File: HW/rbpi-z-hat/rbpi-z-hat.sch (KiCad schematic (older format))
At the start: 0 parts

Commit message: Changes in Sch
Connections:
- net labels added: BQ24313_OUT
- wire segments 66 -> 69
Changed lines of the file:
@@
 $Descr A4 8268 11693 portrait
 encoding utf-8
-Sheet 1 18
+Sheet 1 17
 Title "RasPi Zero NAV Hat"
 Date "2020-08-11"
@@
 $EndSheet
 $Sheet
-S 5200 7900 900  400
-U 5EDADA57
-F0 "MIC5504" 50
-F1 "MIC5504.sch" 50
-F2 "MIC_EN" I L 5200 8100 50
-F3 "MIC_VIN" I L 5200 8000 50
-F4 "MIC_VOUT" I R 6100 8000 50
-F5 "MIC_GND" I L 5200 8200 50
-$EndSheet
-$Sheet
 S 3800 7900 900  400
 U 5EDDEA36
@@
 	3700 8100 3700 8350
 Wire Wire Line
-	4700 8000 5200 8000
+	4700 8000 5300 8000
 $Sheet
 S 5200 750  550  1750
@@
 F0 "SENSORS_POWER" 50
 F1 "SENSORS_POWER.sch" 50
-F2 "SENS_VIN" I L 5200 3850 50
-F3 "SENS_GND" I L 5200 3950 50
-F4 "SENS_EN" I L 5200 4050 50
+F2 "SENS_VIN" I L 5200 3950 50
+F3 "SENS_GND" I L 5200 4050 50
+F4 "SENS_EN" I L 5200 3850 50
 F5 "SENS_VDD" O R 6200 3850 50
 F6 "SENS_FGND" O R 6200 3950 50
@@
 Wire Wire Line
 	2900 3700 3350 3700
+Text Label 5300 8000 2    50   ~ 0
+BQ24313_OUT
+Text Label 4600 3950 0    50   ~ 0
+BQ24313_OUT
+Wire Wire Line
+	5200 3950 4600 3950
+$Comp
+L power:GNDD #PWR?
+U 1 1 610D1539
+P 5050 4100
+F 0 "#PWR?" H 5050 3850 50  0001 C CNN
+F 1 "GNDD" H 5054 3945 50  0000 C CNN
+F 2 "" H 5050 4100 50  0001 C CNN
+F 3 "" H 5050 4100 50  0001 C CNN
+	1    5050 4100
+	1    0    0    -1
+$EndComp
+Wire Wire Line
+	5050 4050 5050 4100
+Wire Wire Line
+	5200 4050 5050 4050
 $EndSCHEMATC

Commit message: Changes in Schematics
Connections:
- net labels added: PCA_nOE, SENSORS_EN
- wire segments 69 -> 67
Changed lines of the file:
@@
 F7 "SPI0_MISO" I R 2900 3600 50
 F8 "SPI0_SCLK" O R 2900 3700 50
-F9 "SPI0_CE0" O R 2900 3800 50
-F10 "GPIO_4" T R 2900 4400 50
-F11 "GPIO_0_HAT_SDA" B R 2900 3250 50
-F12 "GPIO_5" T R 2900 4500 50
-F13 "GPIO_6" T R 2900 4600 50
-F14 "GPIO_13" T R 2900 4700 50
-F15 "GPIO_26" T R 2900 5100 50
-F16 "GPIO_1_HAT_SCL" O R 2900 3350 50
-F17 "GPIO_12" T R 2900 4800 50
-F18 "SPI1_MISO" I R 2900 3950 50
-F19 "SPI1_SCLK" O R 2900 4150 50
-F20 "SPI1_CE2" O R 2900 4250 50
-F21 "SPI1_MOSI" O R 2900 4050 50
-F22 "GPIO_19" T R 2900 4900 50
-F23 "GPIO_22" T R 2900 5000 50
-F24 "UART_RTS" O R 2900 2750 50
-F25 "UART_CTS" I R 2900 2850 50
+F9 "GPIO_0_HAT_SDA" B R 2900 3250 50
+F10 "GPIO_5" T R 2900 4500 50
+F11 "GPIO_6" T R 2900 4600 50
+F12 "GPIO_13" T R 2900 4700 50
+F13 "GPIO_26" T R 2900 5100 50
+F14 "GPIO_1_HAT_SCL" O R 2900 3350 50
+F15 "GPIO_12" T R 2900 4800 50
+F16 "GPIO_19" T R 2900 4900 50
+F17 "GPIO_22" T R 2900 5000 50
+F18 "UART_RTS" O R 2900 2750 50
+F19 "UART_CTS" I R 2900 2850 50
+F20 "GPIO_4" T R 2900 4400 50
+F21 "SBUS_INPUT_RAW" I R 2900 4200 50
+F22 "SPI0_CE0" O R 2900 3800 50
 $EndSheet
 $Sheet
@@
 F6 "ICM_INT1" O L 5200 1450 50
 F7 "ICM_INT2" O L 5200 1550 50
-F8 "LSM_DEN" O L 5200 1650 50
-F9 "LSM_INT1" O L 5200 1750 50
-F10 "LSM_INT2" O L 5200 1850 50
-F11 "LSM_INT3" O L 5200 1950 50
-F12 "LSM_INT4" O L 5200 2050 50
-F13 "IMU_MOSI" I L 5200 850 50
-F14 "IMU_MISO" O L 5200 950 50
-F15 "IMU_SCK" I L 5200 1050 50
+F8 "LSM_INT1" O L 5200 1750 50
+F9 "LSM_INT2" O L 5200 1850 50
+F10 "LSM_INT3" O L 5200 1950 50
+F11 "LSM_INT4" O L 5200 2050 50
+F12 "IMU_MOSI" I L 5200 850 50
+F13 "IMU_MISO" O L 5200 950 50
+F14 "IMU_SCK" I L 5200 1050 50
+F15 "LSM_DEN" I L 5200 1650 50
 $EndSheet
 Wire Wire Line
@@
 	5200 2400 4750 2400
 Wire Wire Line
-	5200 2800 5000 2800
-Wire Wire Line
-	5200 2900 5000 2900
-Wire Wire Line
-	5200 3000 5000 3000
-Wire Wire Line
 	5200 3100 5000 3100
 Wire Wire Line
@@
 	5200 3350 4700 3350
 Wire Wire Line
-	5200 4750 5000 4750
+	5200 4750 4700 4750
 Wire Wire Line
 	5200 5600 5000 5600
@@
 Wire Wire Line
 	2900 3350 3350 3350
-Wire Wire Line
-	2900 3800 3350 3800
-Wire Wire Line
-	2900 3950 3350 3950
-Wire Wire Line
-	2900 4050 3350 4050
-Wire Wire Line
-	2900 4150 3350 4150
-Wire Wire Line
-	2900 4250 3350 4250
 Text Label 3350 2550 2    50   ~ 0
 UART_TX
@@
 	5200 3950 4600 3950
 $Comp
-L power:GNDD #PWR?
+L power:GNDD #PWR0135
 U 1 1 610D1539
 P 5050 4100
-F 0 "#PWR?" H 5050 3850 50  0001 C CNN
+F 0 "#PWR0135" H 5050 3850 50  0001 C CNN
 F 1 "GNDD" H 5054 3945 50  0000 C CNN
 F 2 "" H 5050 4100 50  0001 C CNN
@@
 Wire Wire Line
 	5200 4050 5050 4050
+Text Label 4600 3850 0    50   ~ 0
+SENSORS_EN
+Wire Wire Line
+	5200 3850 4600 3850
+Text Label 3600 5100 2    50   ~ 0
+SENSORS_EN
+Wire Wire Line
+	3000 5100 3600 5100
+Text Label 4700 4750 0    50   ~ 0
+PCA_nOE
+Wire Wire Line
+	3000 5000 3600 5000
+Text Label 3600 5000 2    50   ~ 0
+PCA_nOE
+Text Label 4700 2800 0    50   ~ 0
+SENS_MOSI
+Text Label 4700 2900 0    50   ~ 0
+SENS_MISO
+Text Label 4700 3000 0    50   ~ 0
+SENS_SCK
+Wire Wire Line
+	4700 2800 5200 2800
+Wire Wire Line
+	4700 2900 5200 2900
+Wire Wire Line
+	4700 3000 5200 3000
 $EndSCHEMATC

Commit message: Changes in Schematics
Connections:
- net labels added: BMP_nCS, LSM_nCS
- wire segments 67 -> 69
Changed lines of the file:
@@
 F21 "SBUS_INPUT_RAW" I R 2900 4200 50
 F22 "SPI0_CE0" O R 2900 3800 50
+F23 "SPI0_CE1" O R 2900 3900 50
 $EndSheet
 $Sheet
@@
 	5200 2400 4750 2400
 Wire Wire Line
-	5200 3100 5000 3100
-Wire Wire Line
-	5200 3200 5000 3200
+	5200 3100 4700 3100
+Wire Wire Line
+	5200 3200 4700 3200
 Wire Wire Line
 	5200 3350 4700 3350
@@
 Wire Wire Line
 	4700 3000 5200 3000
+Text Label 4750 1200 0    50   ~ 0
+LSM_nCS
+Text Label 3350 3800 2    50   ~ 0
+LSM_nCS
+Wire Wire Line
+	2900 3800 3350 3800
+Text Label 4700 3200 0    50   ~ 0
+BMP_nCS
+Text Label 3350 3900 2    50   ~ 0
+BMP_nCS
+Wire Wire Line
+	2900 3900 3350 3900
 $EndSCHEMATC

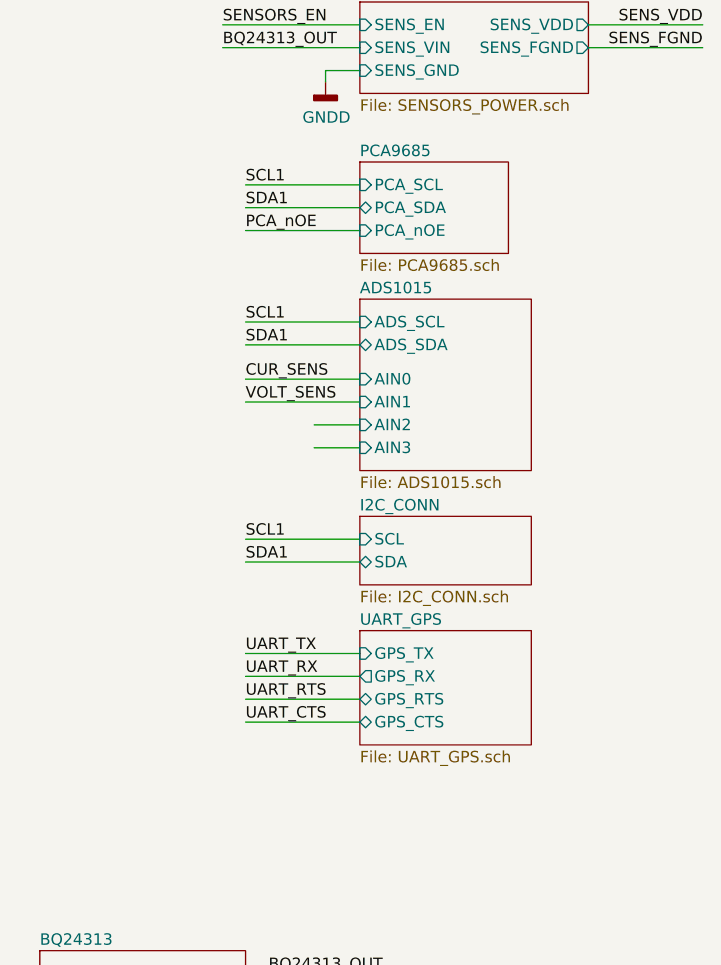
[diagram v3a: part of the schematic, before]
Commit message: Updated PCA9685.sch
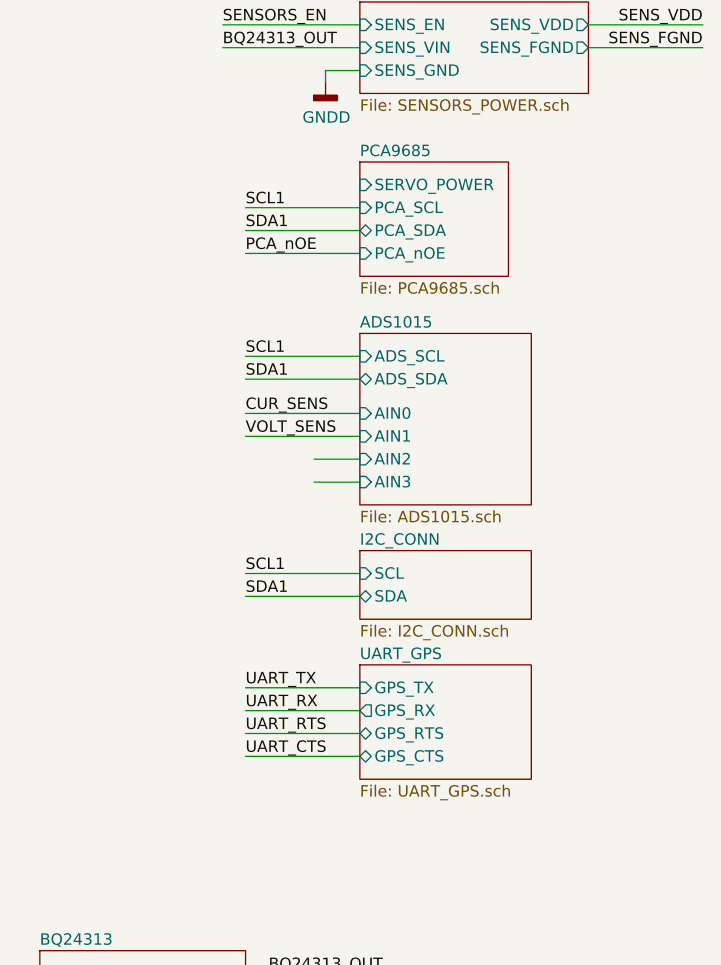
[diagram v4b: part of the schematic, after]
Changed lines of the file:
@@
 $EndDescr
 $Sheet
-S 5200 4450 650  400
+S 5200 4450 650  500
 U 5ED666AD
 F0 "PCA9685" 50
 F1 "PCA9685.sch" 50
-F2 "PCA_SCL" I L 5200 4550 50
-F3 "PCA_SDA" B L 5200 4650 50
-F4 "PCA_nOE" I L 5200 4750 50
+F2 "PCA_SCL" I L 5200 4650 50
+F3 "PCA_SDA" B L 5200 4750 50
+F4 "PCA_nOE" I L 5200 4850 50
+F5 "SERVO_POWER" I L 5200 4550 50
 $EndSheet
 $Sheet
@@
 $EndSheet
 $Sheet
-S 5200 6500 750  500
+S 5200 6650 750  500
 U 5F0378CD
 F0 "UART_GPS" 50
 F1 "UART_GPS.sch" 50
-F2 "GPS_TX" I L 5200 6600 50
-F3 "GPS_RX" O L 5200 6700 50
-F4 "GPS_CTS" B L 5200 6900 50
-F5 "GPS_RTS" B L 5200 6800 50
-$EndSheet
-$Sheet
-S 5200 6000 750  300
+F2 "GPS_TX" I L 5200 6750 50
+F3 "GPS_RX" O L 5200 6850 50
+F4 "GPS_CTS" B L 5200 7050 50
+F5 "GPS_RTS" B L 5200 6950 50
+$EndSheet
+$Sheet
+S 5200 6150 750  300
 U 5EDD13AE
 F0 "I2C_CONN" 50
 F1 "I2C_CONN.sch" 50
-F2 "SCL" I L 5200 6100 50
-F3 "SDA" B L 5200 6200 50
-$EndSheet
-$Sheet
-S 5200 5050 750  750
+F2 "SCL" I L 5200 6250 50
+F3 "SDA" B L 5200 6350 50
+$EndSheet
+$Sheet
+S 5200 5200 750  750
 U 5EF0850C
 F0 "ADS1015" 50
 F1 "ADS1015.sch" 50
-F2 "AIN0" I L 5200 5400 50
-F3 "AIN1" I L 5200 5500 50
-F4 "AIN2" I L 5200 5600 50
-F5 "AIN3" I L 5200 5700 50
-F6 "ADS_SCL" I L 5200 5150 50
-F7 "ADS_SDA" B L 5200 5250 50
+F2 "AIN0" I L 5200 5550 50
+F3 "AIN1" I L 5200 5650 50
+F4 "AIN2" I L 5200 5750 50
+F5 "AIN3" I L 5200 5850 50
+F6 "ADS_SCL" I L 5200 5300 50
+F7 "ADS_SDA" B L 5200 5400 50
 $EndSheet
 $Sheet
@@
 	5200 3350 4700 3350
 Wire Wire Line
-	5200 4750 4700 4750
-Wire Wire Line
-	5200 5600 5000 5600
-Wire Wire Line
-	5200 5700 5000 5700
+	5200 4850 4700 4850
+Wire Wire Line
+	5200 5750 5000 5750
+Wire Wire Line
+	5200 5850 5000 5850
 Wire Wire Line
 	3050 8100 3550 8100
@@
 Text Label 3550 8200 2    50   ~ 0
 VOLT_SENS
-Text Label 4700 5400 0    50   ~ 0
+Text Label 4700 5550 0    50   ~ 0
 CUR_SENS
-Text Label 4700 5500 0    50   ~ 0
+Text Label 4700 5650 0    50   ~ 0
 VOLT_SENS
 Wire Wire Line
-	4700 5400 5200 5400
-Wire Wire Line
-	4700 5500 5200 5500
+	4700 5550 5200 5550
+Wire Wire Line
+	4700 5650 5200 5650
 Wire Wire Line
 	2900 2550 3350 2550
@@
 Text Label 3350 2850 2    50   ~ 0
 UART_CTS
-Text Label 4700 6600 0    50   ~ 0
+Text Label 4700 6750 0    50   ~ 0
 UART_TX
-Text Label 4700 6700 0    50   ~ 0
+Text Label 4700 6850 0    50   ~ 0
 UART_RX
-Text Label 4700 6800 0    50   ~ 0
+Text Label 4700 6950 0    50   ~ 0
 UART_RTS
-Text Label 4700 6900 0    50   ~ 0
+Text Label 4700 7050 0    50   ~ 0
 UART_CTS
 Wire Wire Line
-	4700 6600 5200 6600
-Wire Wire Line
-	4700 6700 5200 6700
-Wire Wire Line
-	4700 6800 5200 6800
-Wire Wire Line
-	4700 6900 5200 6900
+	4700 6750 5200 6750
+Wire Wire Line
+	4700 6850 5200 6850
+Wire Wire Line
+	4700 6950 5200 6950
+Wire Wire Line
+	4700 7050 5200 7050
 Text Label 3350 3100 2    50   ~ 0
 SDA1
@@
 Text Label 4700 3450 0    50   ~ 0
 SENS_FGND
-Text Label 4700 6200 0    50   ~ 0
+Text Label 4700 6350 0    50   ~ 0
 SDA1
-Text Label 4700 6100 0    50   ~ 0
+Text Label 4700 6250 0    50   ~ 0
 SCL1
 Wire Wire Line
-	4700 6100 5200 6100
-Wire Wire Line
-	4700 6200 5200 6200
+	4700 6250 5200 6250
+Wire Wire Line
+	4700 6350 5200 6350
+Text Label 4700 4750 0    50   ~ 0
+SDA1
 Text Label 4700 4650 0    50   ~ 0
+SCL1
+Wire Wire Line
+	4700 4650 5200 4650
+Wire Wire Line
+	4700 4750 5200 4750
+Text Label 4700 5400 0    50   ~ 0
 SDA1
-Text Label 4700 4550 0    50   ~ 0
+Text Label 4700 5300 0    50   ~ 0
 SCL1
 Wire Wire Line
-	4700 4550 5200 4550
-Wire Wire Line
-	4700 4650 5200 4650
-Text Label 4700 5250 0    50   ~ 0
-SDA1
-Text Label 4700 5150 0    50   ~ 0
-SCL1
-Wire Wire Line
-	4700 5150 5200 5150
-Wire Wire Line
-	4700 5250 5200 5250
+	4700 5300 5200 5300
+Wire Wire Line
+	4700 5400 5200 5400
 Text Label 4750 850  0    50   ~ 0
 SENS_MOSI
@@
 Wire Wire Line
 	3000 5100 3600 5100
-Text Label 4700 4750 0    50   ~ 0
+Text Label 4700 4850 0    50   ~ 0
 PCA_nOE
 Wire Wire Line
